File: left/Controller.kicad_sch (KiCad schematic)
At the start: 35 parts, among them J1 AudioJack4, J10 Conn_01x04, J11 Conn_01x01, J12 Conn_01x02, J13 Conn_01x01, J14 Conn_01x01, J15 Conn_01x01, J16 Conn_01x01, J17 Conn_01x01, J2 Conn_01x01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

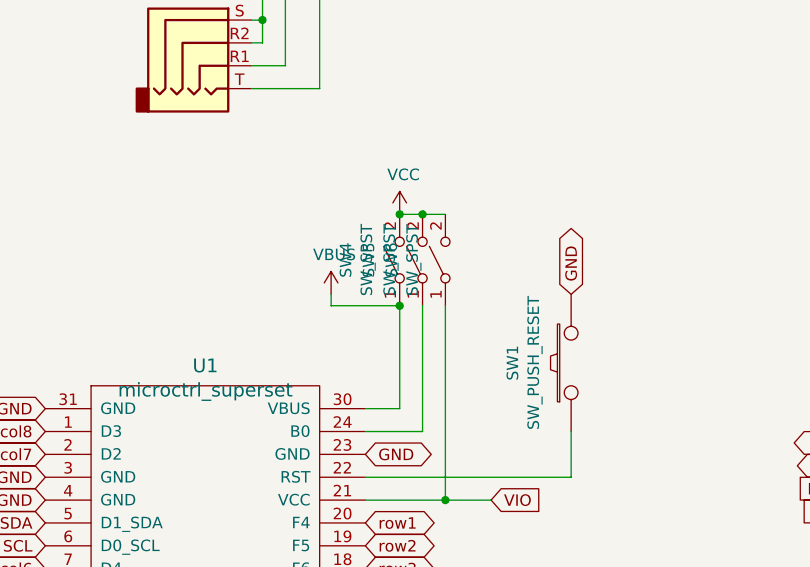
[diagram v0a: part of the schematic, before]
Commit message: Broke out keys into individual components so that the BOM and pick and place are easier to generate.
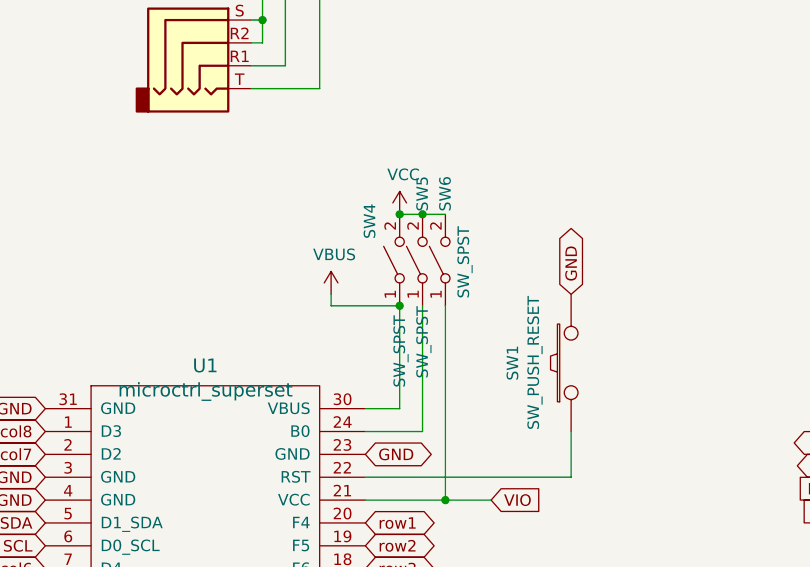
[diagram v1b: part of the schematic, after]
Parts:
- C1, C2, C3, C4, C5, C6: footprint Capacitor_SMD:C_0805_2012Metric_Pad1.15x1.40mm_HandSolder -> Capacitor_SMD:C_0805_2012Metric
- R1, R2, R3, R4, R5, Rext1: footprint Resistor_SMD:R_0603_1608Metric_Pad1.05x0.95mm_HandSolder -> Resistor_SMD:R_0603_1608Metric

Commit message: Kicad 9 upgrade.
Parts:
- C1, C2, C3: value CP -> 0.47 uF; LCSC (none) -> C49955
- C4, C5, C6: value CP -> 0.1 uF; LCSC (none) -> C49678
- J1: LCSC (none) -> C431535
- J11, J17, J2, J3, J5, J6, J7, J9: LCSC (none) -> C2916379
- R1, R2, R4: LCSC (none) -> C25803
- R3, R5: LCSC (none) -> C21190
- Rext1: LCSC (none) -> C4184
- SW1: LCSC (none) -> C99271
- U2: LCSC (none) -> C17348851
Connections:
- no-connect marks 10 -> 11

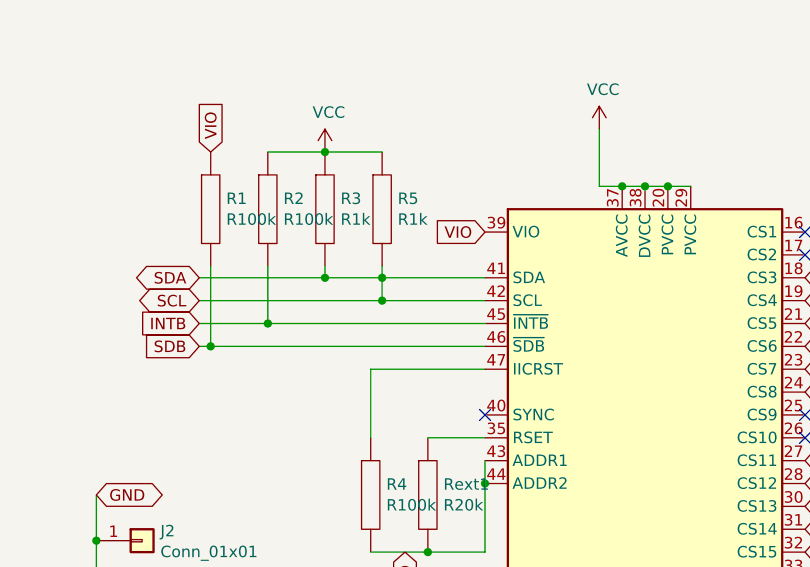
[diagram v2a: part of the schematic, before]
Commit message: Fix SDA/SCL bug
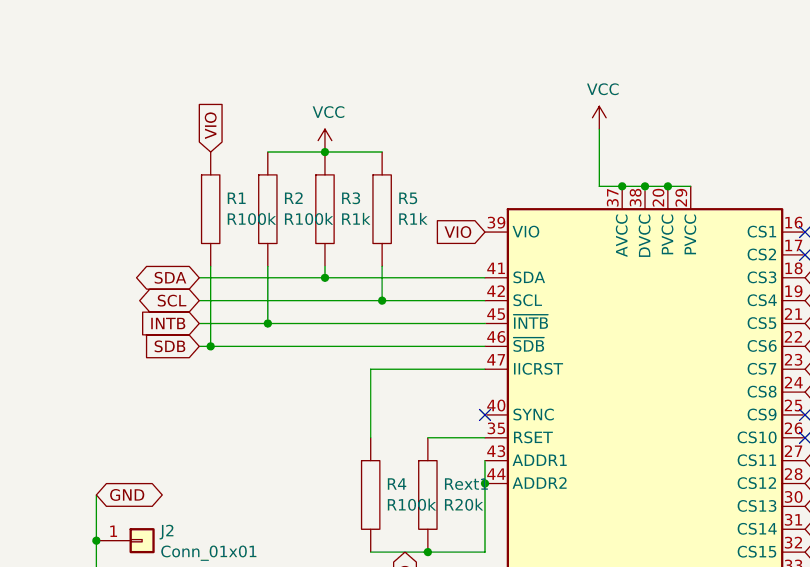
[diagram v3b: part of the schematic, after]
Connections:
- net SCL: no longer J10.1 (Pin_1), R3.2, U1.5 (D1_SDA), U2.41 (SDA)
- new net SDA: J10.1 (Pin_1), R3.2, U1.5 (D1_SDA), U2.41 (SDA)
